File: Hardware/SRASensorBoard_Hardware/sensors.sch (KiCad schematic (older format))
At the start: 70 parts, among them J1 USB_A, Q2 BSS138, Q3 BSS138, Q4 BSS138, Q5 BSS138, Q6 BSS138, U4 FT230XS, U5 TSV911RILT, U6 TSV911RILT

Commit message: rev 2 changes
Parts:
- removed D10, D11, D12, D13, D20, D6, D7, D8: Blue, LED_SMD:LED_0603_1608Metric_Pad1.05x0.95mm_HandSolder, symbol Device:LED
- removed R10, R11, R12, R13, R14, R30, R32, R33, R34, R35, R44, R45, R6, R7, R8, R9: 240, Resistor_SMD:R_0603_1608Metric_Pad1.05x0.95mm_HandSolder, symbol Device:R
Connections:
- net NO_Gas: no longer C14.2, R49.2, U6.1
- new net NO_Ref: C14.2, R49.2, U6.1

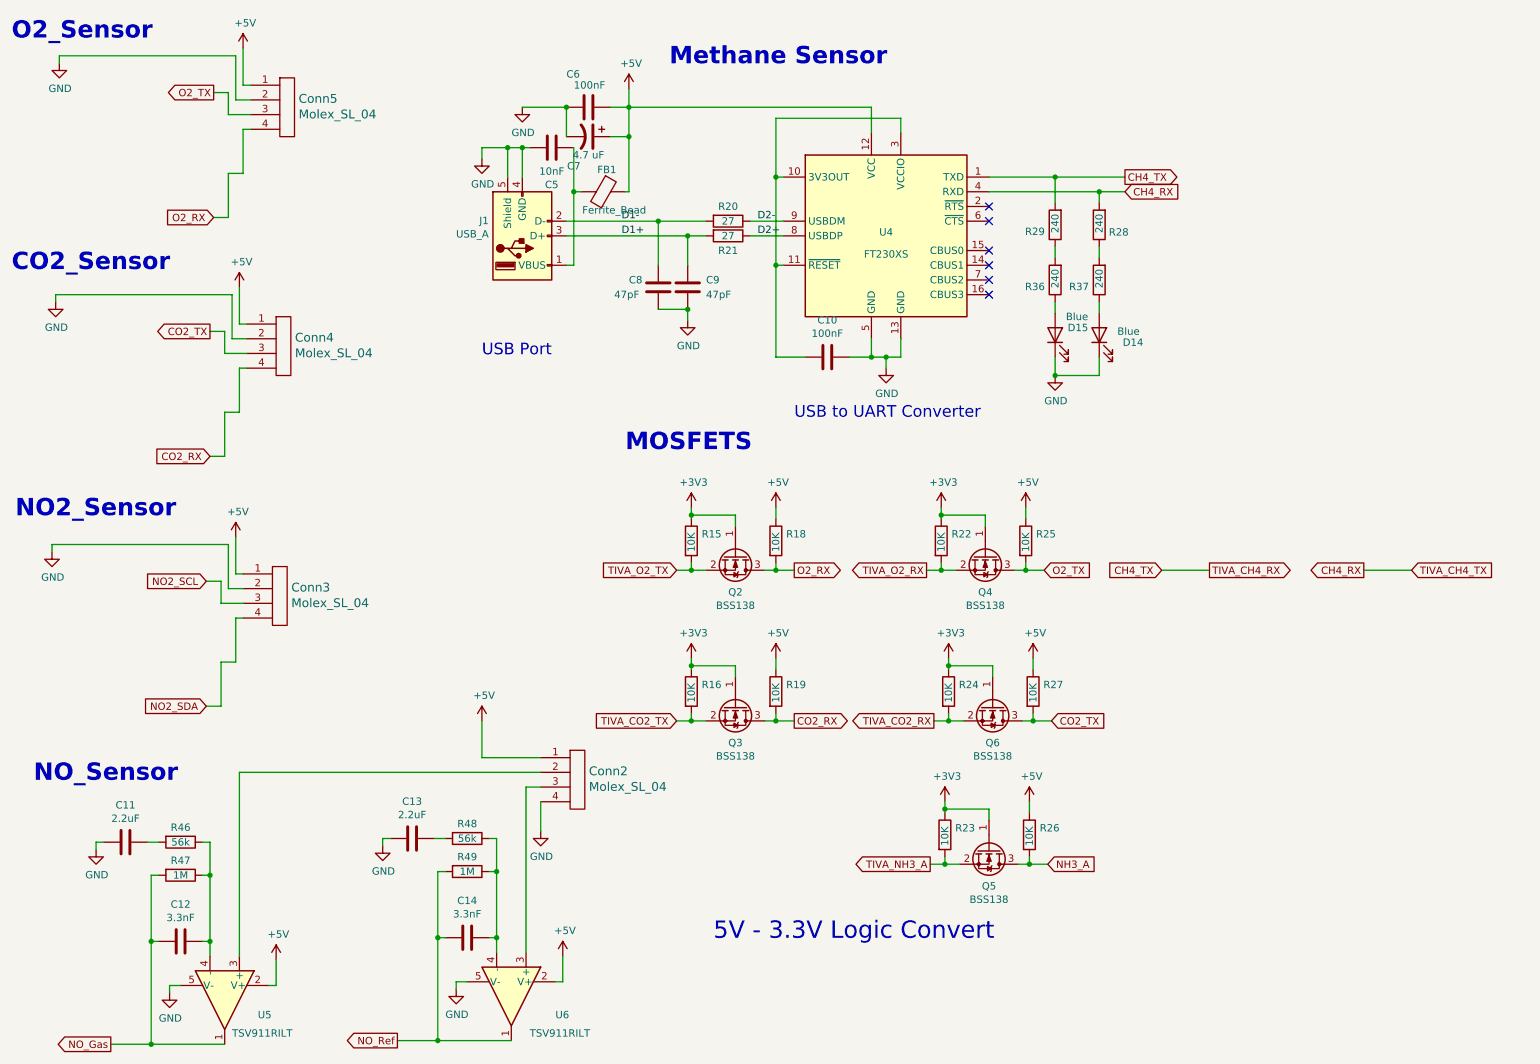
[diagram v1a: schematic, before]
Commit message: changed resistor values
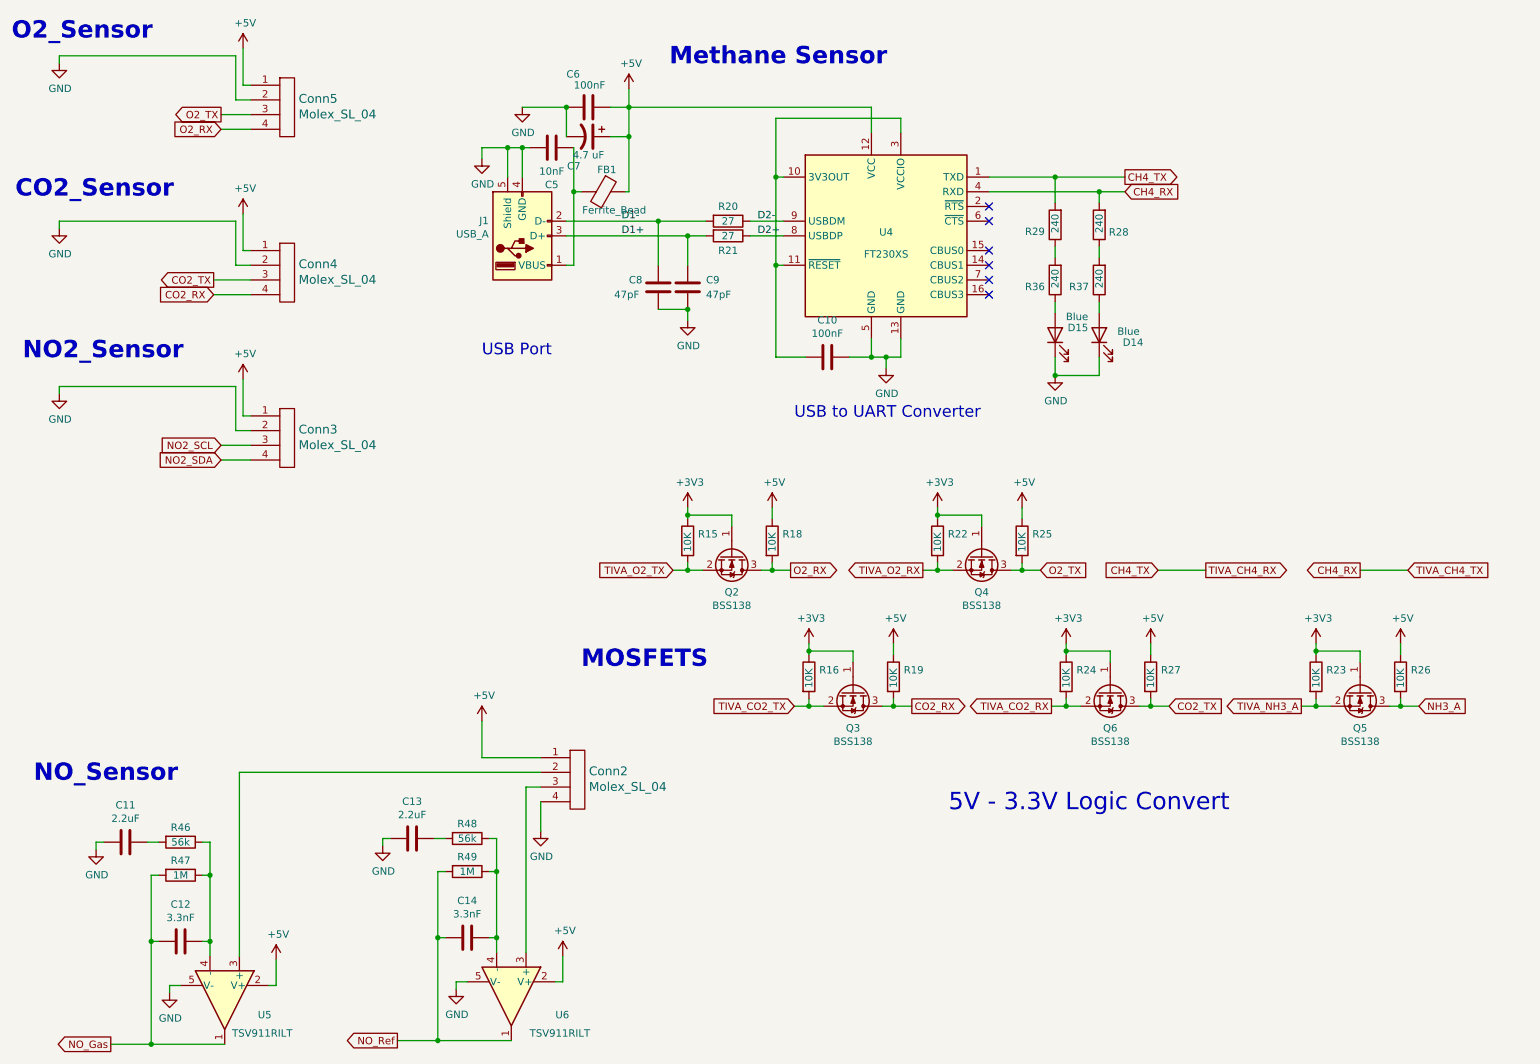
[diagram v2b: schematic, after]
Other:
- moved on the sheet: Conn3, Conn4, Q2, Q3, Q4, Q5, Q6, R15, R16, R18, R19, R22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

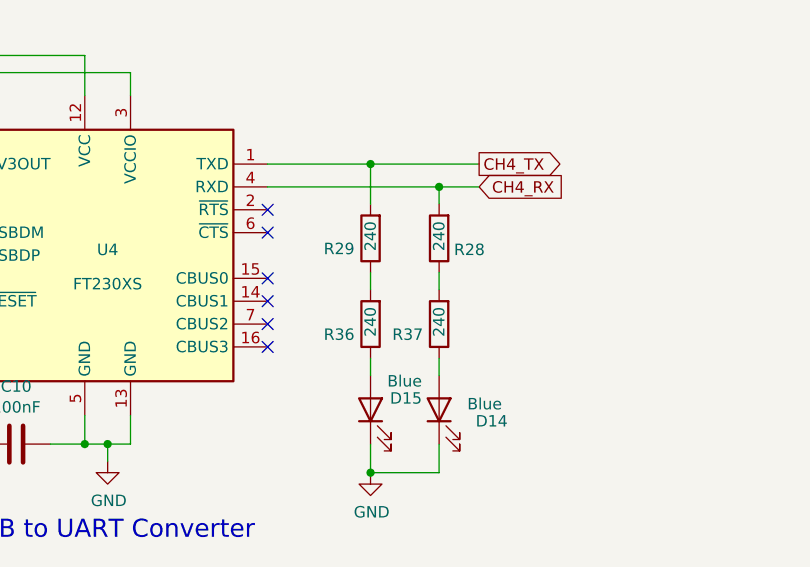
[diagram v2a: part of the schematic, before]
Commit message: updated resistor values and moved via
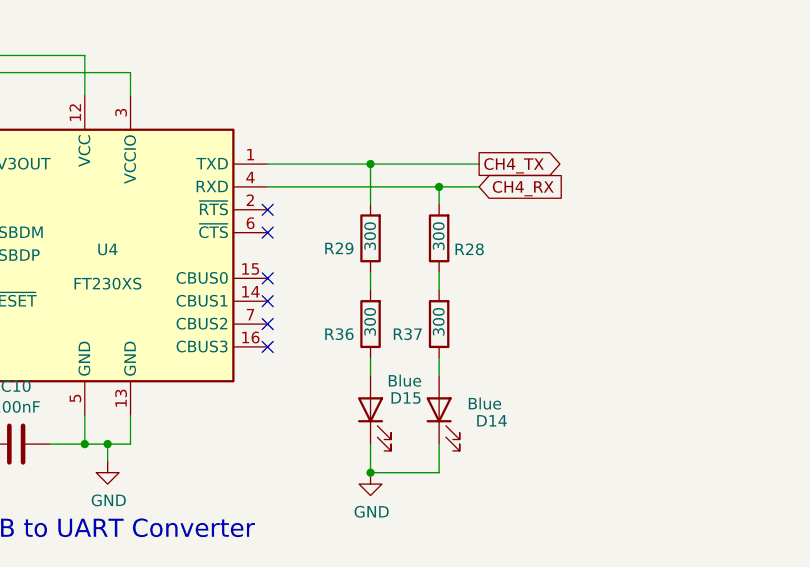
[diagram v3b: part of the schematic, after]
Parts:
- R28, R29, R36, R37: value 240 -> 300
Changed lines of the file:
@@
 	1    0    0    -1
 $EndComp
-Wire Wire Line
-	7950 1825 8125 1825
-Connection ~ 7950 1825
-Wire Wire Line
-	7950 1825 7950 1900
-Wire Wire Line
-	7650 1725 8125 1725
-Connection ~ 7650 1725
-Wire Wire Line
-	7650 1725 7650 1900
-Wire Wire Line
-	7200 1725 7650 1725
-Wire Wire Line
-	7200 1825 7950 1825
-$Comp
-L Device:R R28
-U 1 1 6168B9AC
-P 7950 2050
-F 0 "R28" H 7750 2100 50  0000 L CNN
-F 1 "240" V 7950 1975 50  0000 L CNN
-F 2 "Resistor_SMD:R_0603_1608Metric_Pad1.05x0.95mm_HandSolder" V 7880 2050 50  0001 C CNN
-F 3 "~" H 7950 2050 50  0001 C CNN
-	1    7950 2050
-	-1   0    0    1
-$EndComp
-$Comp
-L Device:R R29
-U 1 1 6168BDE5
-P 7650 2050
-F 0 "R29" H 7720 2096 50  0000 L CNN
-F 1 "240" V 7650 1975 50  0000 L CNN
-F 2 "Resistor_SMD:R_0603_1608Metric_Pad1.05x0.95mm_HandSolder" V 7580 2050 50  0001 C CNN
-F 3 "~" H 7650 2050 50  0001 C CNN
-	1    7650 2050
-	-1   0    0    1
-$EndComp
-$Comp
-L Device:LED D14
-U 1 1 6168C4BA
-P 7950 2800
-F 0 "D14" V 7900 2500 50  0000 L CNN
-F 1 "Blue" V 7975 2525 50  0000 L CNN
-F 2 "LED_SMD:LED_0603_1608Metric_Pad1.05x0.95mm_HandSolder" H 7950 2800 50  0001 C CNN
-F 3 "~" H 7950 2800 50  0001 C CNN
-	1    7950 2800
-	0    -1   -1   0
-$EndComp
-$Comp
-L Device:LED D15
-U 1 1 6168D01D
-P 7650 2800
-F 0 "D15" V 7700 2575 50  0000 L CNN
-F 1 "Blue" V 7775 2575 50  0000 L CNN
-F 2 "LED_SMD:LED_0603_1608Metric_Pad1.05x0.95mm_HandSolder" H 7650 2800 50  0001 C CNN
-F 3 "~" H 7650 2800 50  0001 C CNN
-	1    7650 2800
-	0    -1   -1   0
-$EndComp
-$Comp
-L power:GND #PWR0134
-U 1 1 61690493
-P 7650 3075
-F 0 "#PWR0134" H 7650 2825 50  0001 C CNN
-F 1 "GND" H 7655 2902 50  0000 C CNN
-F 2 "" H 7650 3075 50  0001 C CNN
-F 3 "" H 7650 3075 50  0001 C CNN
-	1    7650 3075
-	1    0    0    -1
-$EndComp
-Wire Wire Line
-	7950 2575 7950 2650
-Wire Wire Line
-	7950 2950 7950 3075
-Wire Wire Line
-	7950 3075 7650 3075
-Wire Wire Line
-	7650 2950 7650 3075
-Connection ~ 7650 3075
-Wire Wire Line
-	7650 2650 7650 2575
 Text GLabel 8125 1825 2    50   Input ~ 0
 CH4_RX
 Text GLabel 8125 1725 2    50   Output ~ 0
 CH4_TX
-$Comp
-L Device:R R36
-U 1 1 61907565
-P 7650 2425
-F 0 "R36" H 7720 2471 50  0000 L CNN
-F 1 "240" V 7650 2350 50  0000 L CNN
-F 2 "Resistor_SMD:R_0603_1608Metric_Pad1.05x0.95mm_HandSolder" V 7580 2425 50  0001 C CNN
-F 3 "~" H 7650 2425 50  0001 C CNN
-	1    7650 2425
-	-1   0    0    1
-$EndComp
-$Comp
-L Device:R R37
-U 1 1 61907863
-P 7950 2425
-F 0 "R37" H 8020 2471 50  0000 L CNN
-F 1 "240" V 7950 2350 50  0000 L CNN
-F 2 "Resistor_SMD:R_0603_1608Metric_Pad1.05x0.95mm_HandSolder" V 7880 2425 50  0001 C CNN
-F 3 "~" H 7950 2425 50  0001 C CNN
-	1    7950 2425
-	-1   0    0    1
-$EndComp
-Wire Wire Line
-	7650 2200 7650 2275
-Wire Wire Line
-	7950 2200 7950 2275
 $Comp
 L power:GND #PWR0130
@@
 Text Notes 6925 6050 0    118  ~ 0
 5V - 3.3V Logic Convert
+Wire Wire Line
+	7200 1725 7650 1725
+Wire Wire Line
+	7650 1725 8125 1725
+Connection ~ 7650 1725
+Wire Wire Line
+	7650 1725 7650 1900
+Wire Wire Line
+	7200 1825 7950 1825
+Wire Wire Line
+	7950 1825 8125 1825
+Connection ~ 7950 1825
+Wire Wire Line
+	7950 1825 7950 1900
+Wire Wire Line
+	7950 2200 7950 2275
+Wire Wire Line
+	7650 2200 7650 2275
+$Comp
+L Device:R R37
+U 1 1 61907863
+P 7950 2425
+F 0 "R37" H 8020 2471 50  0000 L CNN
+F 1 "300" V 7950 2350 50  0000 L CNN
+F 2 "Resistor_SMD:R_0603_1608Metric_Pad1.05x0.95mm_HandSolder" V 7880 2425 50  0001 C CNN
+F 3 "~" H 7950 2425 50  0001 C CNN
+	1    7950 2425
+	-1   0    0    1
+$EndComp
+$Comp
+L Device:R R36
+U 1 1 61907565
+P 7650 2425
+F 0 "R36" H 7720 2471 50  0000 L CNN
+F 1 "300" V 7650 2350 50  0000 L CNN
+F 2 "Resistor_SMD:R_0603_1608Metric_Pad1.05x0.95mm_HandSolder" V 7580 2425 50  0001 C CNN
+F 3 "~" H 7650 2425 50  0001 C CNN
+	1    7650 2425
+	-1   0    0    1
+$EndComp
+Wire Wire Line
+	7650 2650 7650 2575
+Wire Wire Line
+	7650 2950 7650 3075
+Wire Wire Line
+	7950 3075 7650 3075
+Wire Wire Line
+	7950 2950 7950 3075
+Wire Wire Line
+	7950 2575 7950 2650
+Connection ~ 7650 3075
+$Comp
+L power:GND #PWR0134
+U 1 1 61690493
+P 7650 3075
+F 0 "#PWR0134" H 7650 2825 50  0001 C CNN
+F 1 "GND" H 7655 2902 50  0000 C CNN
+F 2 "" H 7650 3075 50  0001 C CNN
+F 3 "" H 7650 3075 50  0001 C CNN
+	1    7650 3075
+	1    0    0    -1
+$EndComp
+$Comp
+L Device:LED D15
+U 1 1 6168D01D
+P 7650 2800
+F 0 "D15" V 7700 2575 50  0000 L CNN
+F 1 "Blue" V 7775 2575 50  0000 L CNN
+F 2 "LED_SMD:LED_0603_1608Metric_Pad1.05x0.95mm_HandSolder" H 7650 2800 50  0001 C CNN
+F 3 "~" H 7650 2800 50  0001 C CNN
+	1    7650 2800
+	0    -1   -1   0
+$EndComp
+$Comp
+L Device:LED D14
+U 1 1 6168C4BA
+P 7950 2800
+F 0 "D14" V 7900 2500 50  0000 L CNN
+F 1 "Blue" V 7975 2525 50  0000 L CNN
+F 2 "LED_SMD:LED_0603_1608Metric_Pad1.05x0.95mm_HandSolder" H 7950 2800 50  0001 C CNN
+F 3 "~" H 7950 2800 50  0001 C CNN
+	1    7950 2800
+	0    -1   -1   0
+$EndComp
+$Comp
+L Device:R R29
+U 1 1 6168BDE5
+P 7650 2050
+F 0 "R29" H 7720 2096 50  0000 L CNN
+F 1 "300" V 7650 1975 50  0000 L CNN
+F 2 "Resistor_SMD:R_0603_1608Metric_Pad1.05x0.95mm_HandSolder" V 7580 2050 50  0001 C CNN
+F 3 "~" H 7650 2050 50  0001 C CNN
+	1    7650 2050
+	-1   0    0    1
+$EndComp
+$Comp
+L Device:R R28
+U 1 1 6168B9AC
+P 7950 2050
+F 0 "R28" H 7750 2100 50  0000 L CNN
+F 1 "300" V 7950 1975 50  0000 L CNN
+F 2 "Resistor_SMD:R_0603_1608Metric_Pad1.05x0.95mm_HandSolder" V 7880 2050 50  0001 C CNN
+F 3 "~" H 7950 2050 50  0001 C CNN
+	1    7950 2050
+	-1   0    0    1
+$EndComp
 $EndSCHEMATC

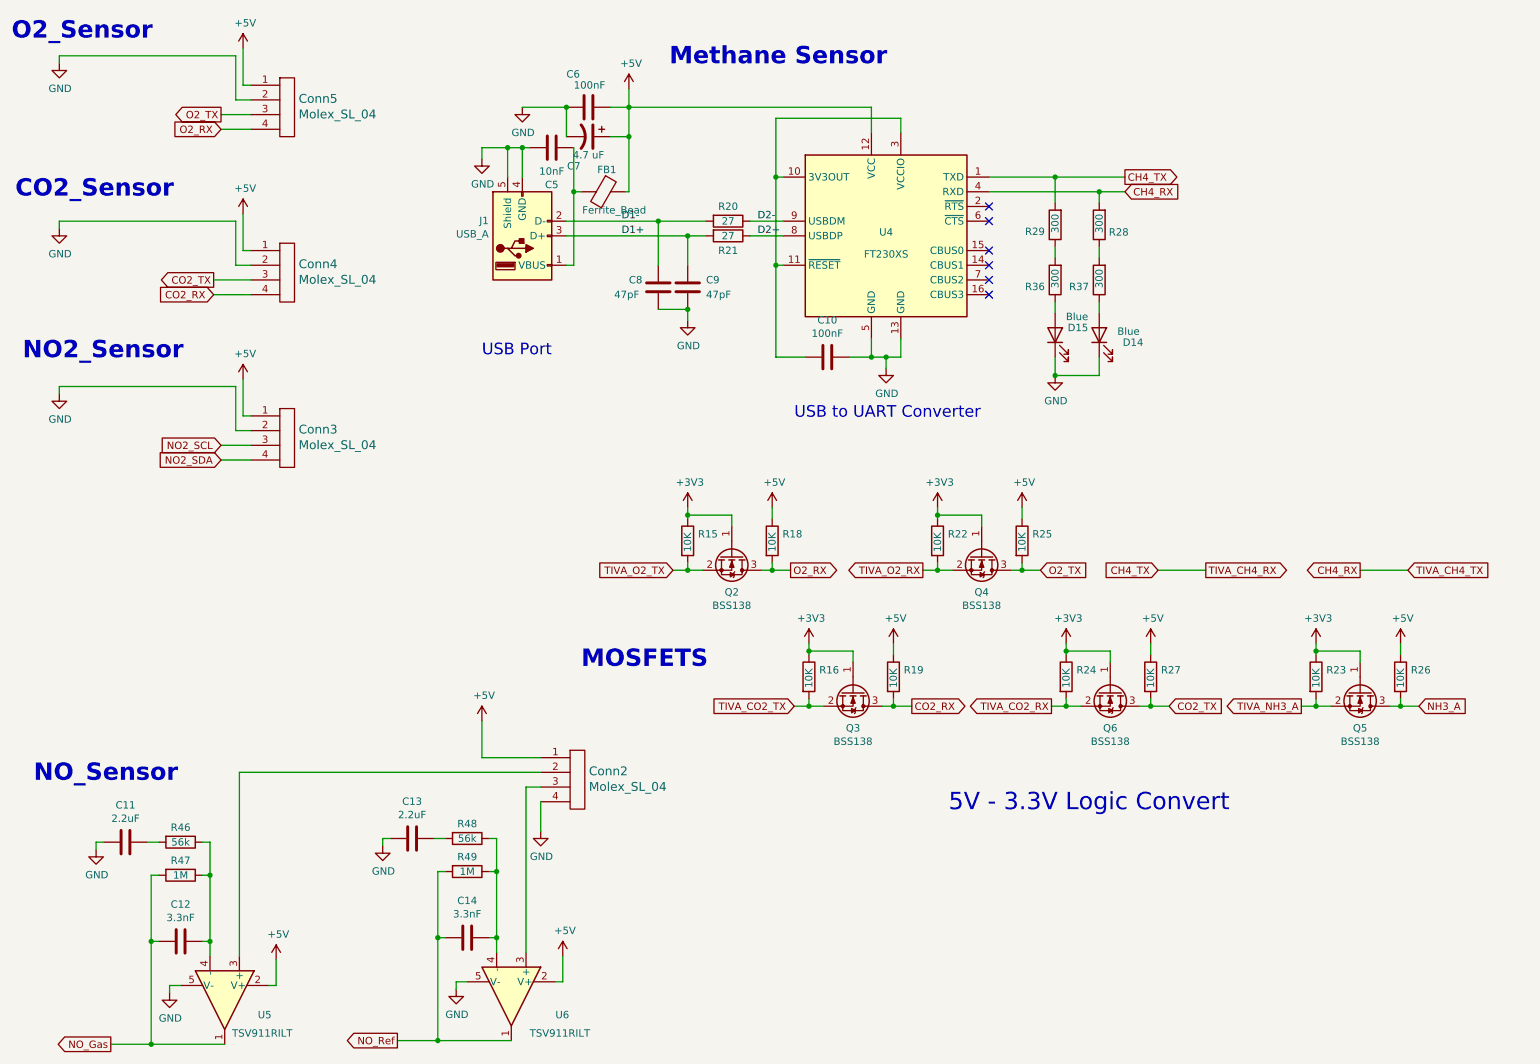
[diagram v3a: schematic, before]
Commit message: added board mounts and did rev 2 changes
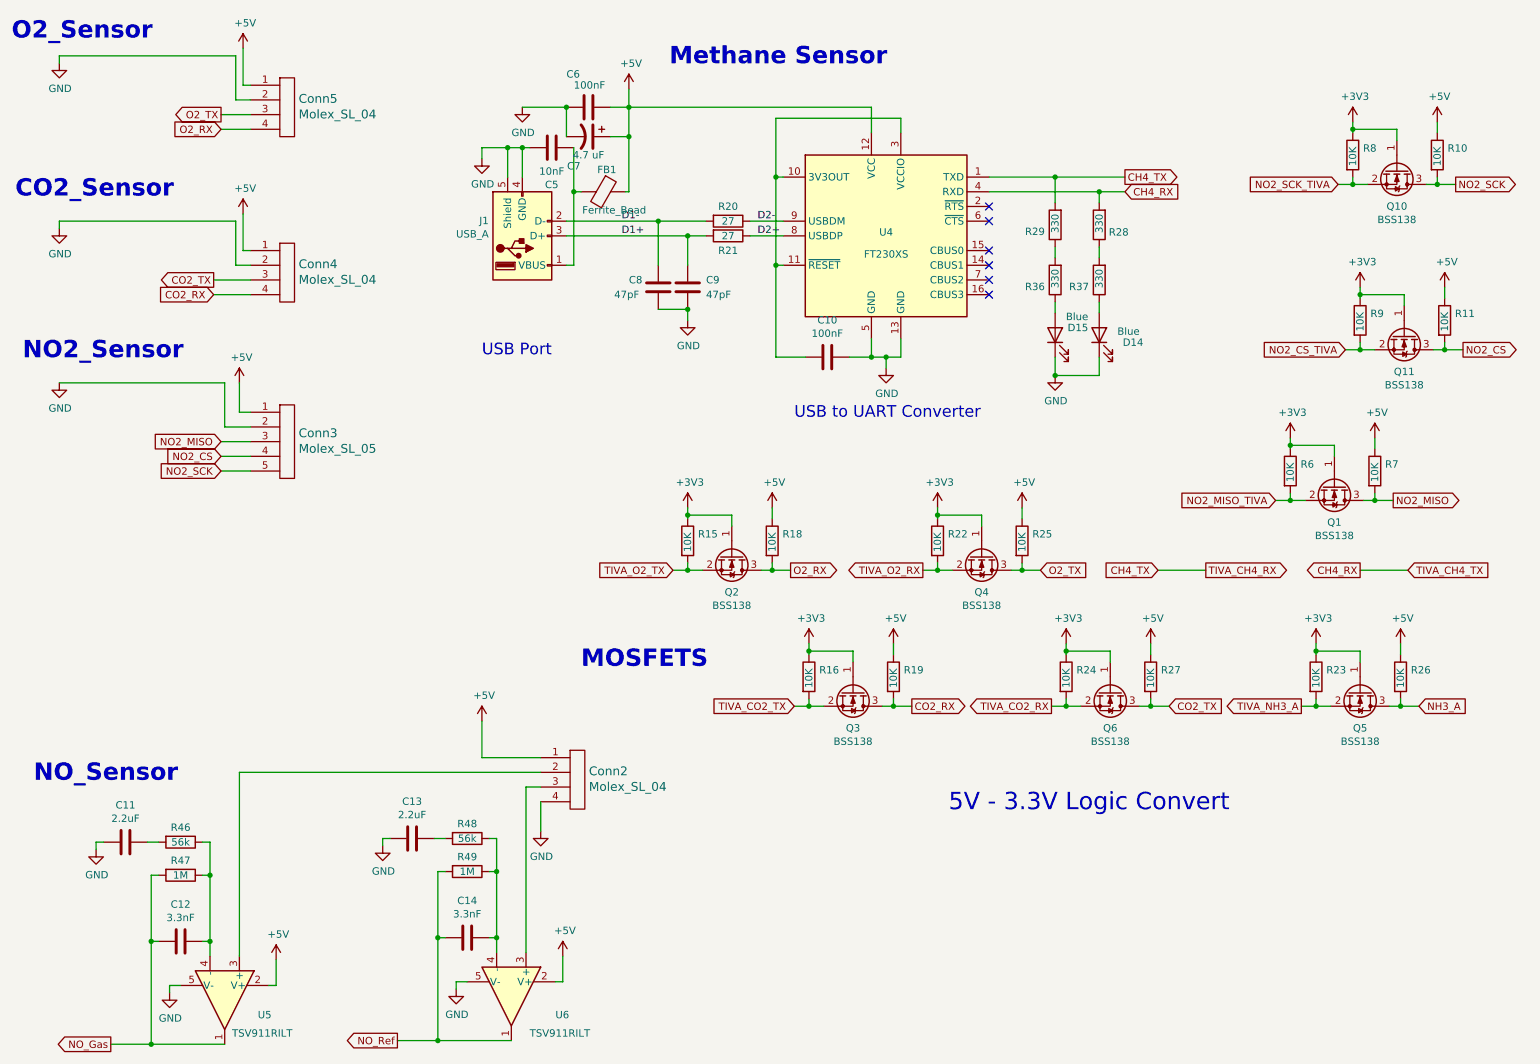
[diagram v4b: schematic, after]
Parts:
- removed Conn3: Molex_SL_04, MRDT_Connectors:MOLEX_SL_04_Horizontal, symbol MRDT_Connectors:Molex_SL_04
- added Conn3: Molex_SL_05, MRDT_Connectors:MOLEX_SL_05_Horizontal, symbol MRDT_Connectors:Molex_SL_05
- added Q1, Q10, Q11: BSS138, Package_TO_SOT_SMD:SOT-23, symbol Transistor_FET:BSS138
- added R10, R11, R6, R7, R8, R9: 10K, Resistor_SMD:R_0603_1608Metric_Pad0.98x0.95mm_HandSolder, symbol Device:R
- R15, R16, R18, R19, R20, R21, R22, R23, R24, R25, R26, R27: footprint Resistor_SMD:R_0603_1608Metric_Pad1.05x0.95mm_HandSolder -> Resistor_SMD:R_0603_1608Metric_Pad0.98x0.95mm_HandSolder
- R28, R29, R36, R37: value 300 -> 330; footprint Resistor_SMD:R_0603_1608Metric_Pad1.05x0.95mm_HandSolder -> Resistor_SMD:R_0603_1608Metric_Pad0.98x0.95mm_HandSolder
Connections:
- net +3V3: now also Q1.1 (G), Q10.1 (G), Q11.1 (G), R6.1, R8.1, R9.1
- net +5V: now also Conn3.1, R10.1, R11.1, R7.1
- net GND: now also Conn3.2
- new net NO2_CS: Conn3.4, Q11.3 (D), R11.2
- new net NO2_CS_TIVA: Q11.2 (S), R9.2
- new net NO2_MISO: Conn3.3, Q1.3 (D), R7.2
- new net NO2_MISO_TIVA: Q1.2 (S), R6.2
- new net NO2_SCK: Conn3.5, Q10.3 (D), R10.2
- new net NO2_SCK_TIVA: Q10.2 (S), R8.2
